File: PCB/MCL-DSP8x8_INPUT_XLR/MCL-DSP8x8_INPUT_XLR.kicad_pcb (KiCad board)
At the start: 2 copper layers, 60 x 40 mm, 11 parts, among them J1 Conn_01x05

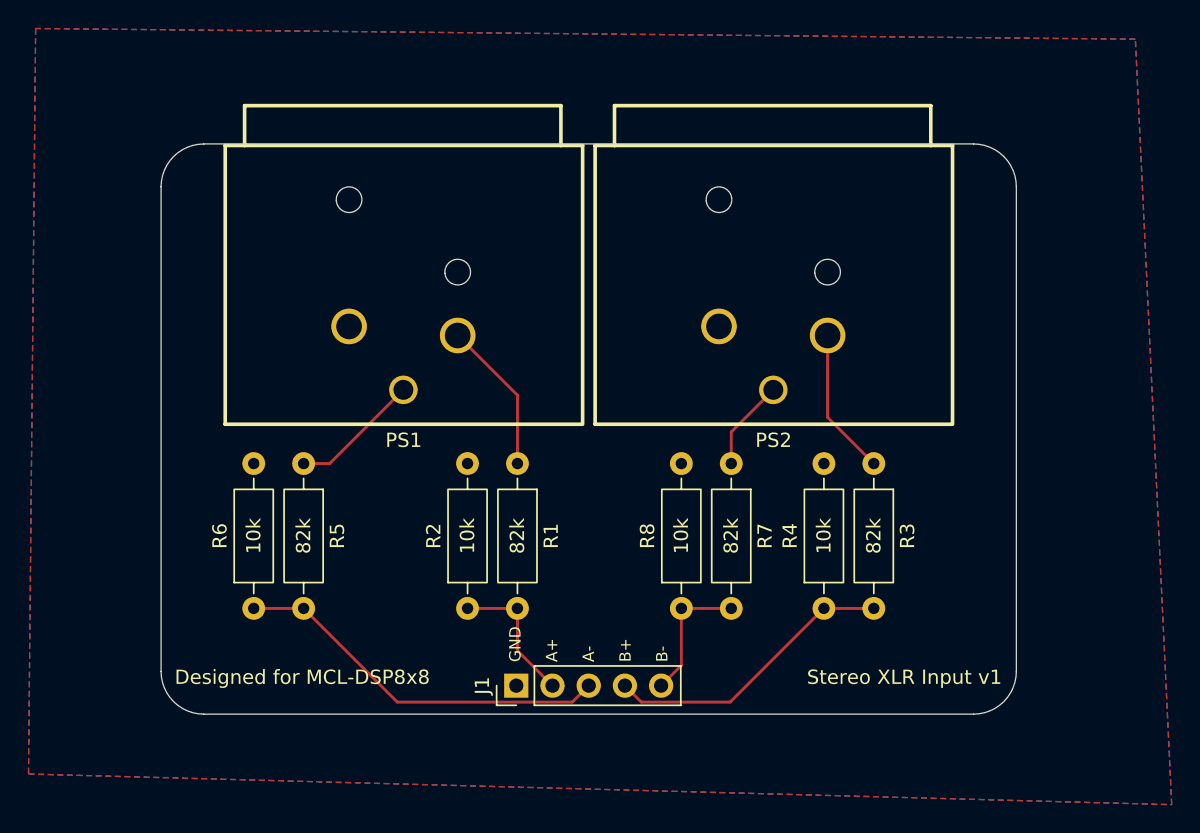
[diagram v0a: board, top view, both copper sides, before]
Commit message: Added DC polarity indicator to main board, created RCA and XLR input/output
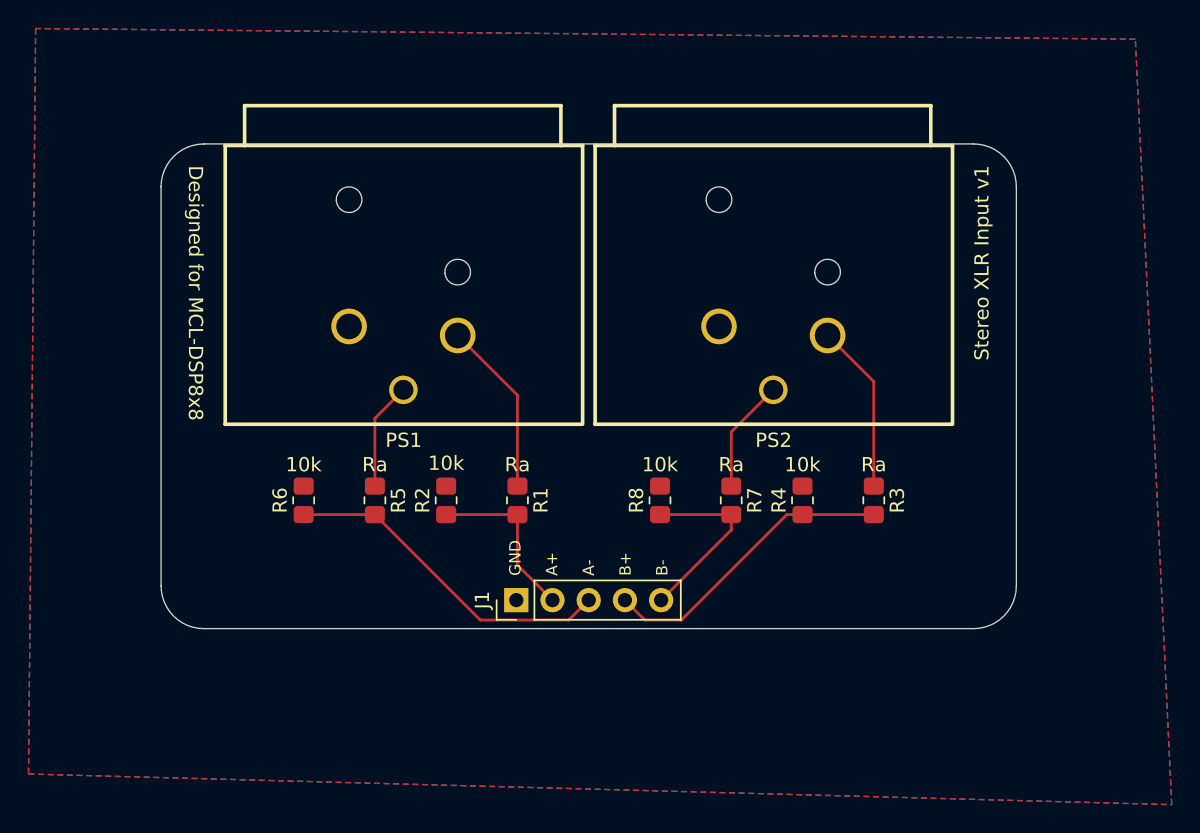
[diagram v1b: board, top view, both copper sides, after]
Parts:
- R1, R2, R3, R4, R5, R6, R7, R8: footprint Resistor_THT:R_Axial_DIN0207_L6.3mm_D2.5mm_P10.16mm_Horizontal -> Resistor_SMD:R_0805_2012Metric_Pad1.20x1.40mm_HandSolder
- moved R6 8.35 mm to (40.0, 55.0)
- moved R2 7.73 mm to (50.0, 55.0)
- moved R4 7.73 mm to (75.0, 55.0)
- moved R8 7.73 mm to (65.0, 55.0)
- moved J1 6.00 mm to (54.9, 62.0)
- moved R5 5.63 mm to (45.0, 55.0)
- moved R1 2.58 mm to (55.0, 55.0)
- moved R3 2.58 mm to (80.0, 55.0)
- moved R7 2.58 mm to (70.0, 55.0)
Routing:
- net /IN_B-: track 9.51 -> 13.0 mm
- net /IN_A-: track 26.7 -> 23.6 mm
- net /IN_A+: track 9.94 -> 12.0 mm
- net /XLR_2+: track 10.3 -> 11.9 mm
- net /XLR_2-: track 6.39 -> 7.97 mm
- net /XLR_1+: track 10.7 -> 12.3 mm
- net /XLR_1-: track 9.14 -> 7.58 mm
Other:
- board size 60 x 40 mm -> 60 x 34 mm
- board text added: "Ra"
- board text added: "Ra 82kΩ -> -20dB 0Ω -> -0dB"
- board text removed: "82k"
- board text removed: "82k resistors give -20dB attenuation. Replace with 0 ohm resistors for 0dB attenuation"
